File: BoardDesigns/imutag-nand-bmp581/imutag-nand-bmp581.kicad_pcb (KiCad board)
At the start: 4 copper layers, 21.5 x 11.5 mm, 36 parts, among them J201 CONN_02X04, J301 Conn_01x01, J302 Conn_01x01, J303 Conn_01x01, J304 Conn_01x01, J401 CONN_01X02, Q501 PMBT2222AMBYL, U1 TPS22916BYFPR, U2 BMM350, U3 BMP581, U302 stm32U375, U4 TPS7A02185PDQNR, U5 LSM6DSV, U501 RV-3028-C8, U6 GD5F2GM7REYIGR

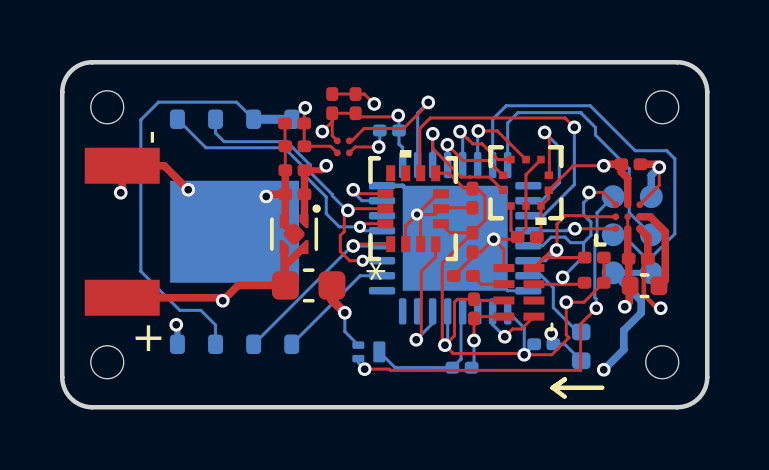
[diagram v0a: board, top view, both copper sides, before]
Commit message: imutag-nand-bmp581: fab-ready for PCBWay, plus stale-project cleanup
Design review round 2, covering the PCBWay fabrication package that did not
exist at the 2026-08-26 review. Closed ready to fabricate.

Board fixes
- Inner planes were flush with the routed profile: In1.Cu (+1V8) and In2.Cu
  (GND) both sat 0.0005 mm from the edge, separated by 0.08 mm of core, with a
  credible burr path from the regulated rail to ground. Invisible to DRC because
  min_copper_edge_clearance was 0. Now 0.3005 mm, rule set to 0.3 and enforced.
- Via annular ring raised 0.1016 -> 0.1524 mm (4.00 -> 6.00 mil) on all 44 vias
  to meet PCBWay's published minimum: pad 0.5048 / drill 0.20, now a single
  drill tool. Shrinking the drill is what buys the ring here; pad growth fails
  against the zones' 0.508 mm connect_pads clearance.
- C4 re-sourced to GRM155Z71A225KE01D (2.2 uF 10 V X7R 0402, LCSC C2997286).
  Bosch's recommended TDK CGB4B3X7R0J225K055AB is obsolete and is an 0805, so it
  was never a drop-in for the 0402 land.
- RV-3028-C8 footprint silk raised to 0.15 mm.

Verified: DRC 0 violations / 0 unconnected / 0 parity; ERC 1 accepted VBAT/VIN
warning; PTH 44 = via count, NPTH 4 = J301-J304; 15 BOM lines / 30 placements
matching the CPL exactly, every line with MPN and LCSC. The 10-01-52 export is
confirmed to match the board on disk.

Production package
- Only the final export, 2026-09-01-10-01-52, is kept; six superseded ones are
  pruned.
- Its gerber archive is committed with `git add -f`, overriding the repo-wide
  *.zip rule in BoardDesigns/.gitignore. Without that the commit would carry
  only the BOM, CPL and netlist, and the package actually sent to the fab would
  not be reproducible: plugin output is not byte-identical to a kicad-cli
  re-plot, so the board file alone does not pin it down. 46 kB.

Stale BitTagNG project files removed repo-wide
- analysis/2026-08-26_1027-2/pcb.json recorded rules_source as
  BitTagNG-LIS2DU12.kicad_pcb-back.kicad_pro, so every rule-deri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
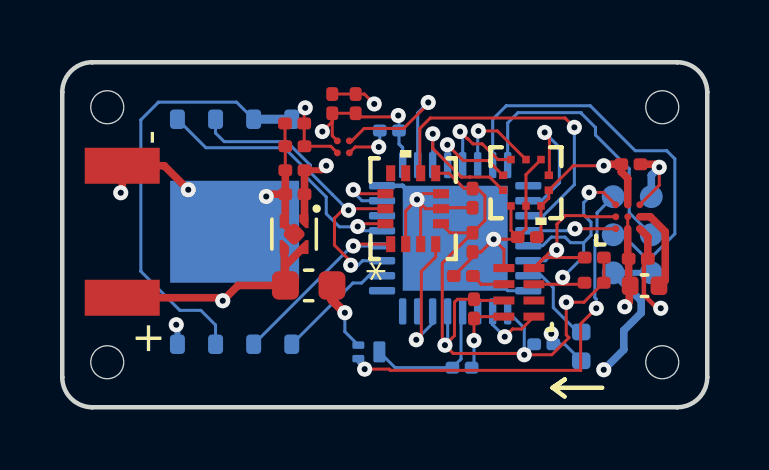
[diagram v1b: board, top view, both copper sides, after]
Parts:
- U501: value RV-3028-C8 -> RV-3028-C8-32.768kHz-1PPM-TA-QC
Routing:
- net GND: track 48.9 -> 49.9 mm
